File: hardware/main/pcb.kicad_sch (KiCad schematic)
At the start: 22 parts, among them J1 Conn_01x02_Socket, J2 Conn_01x02_Socket

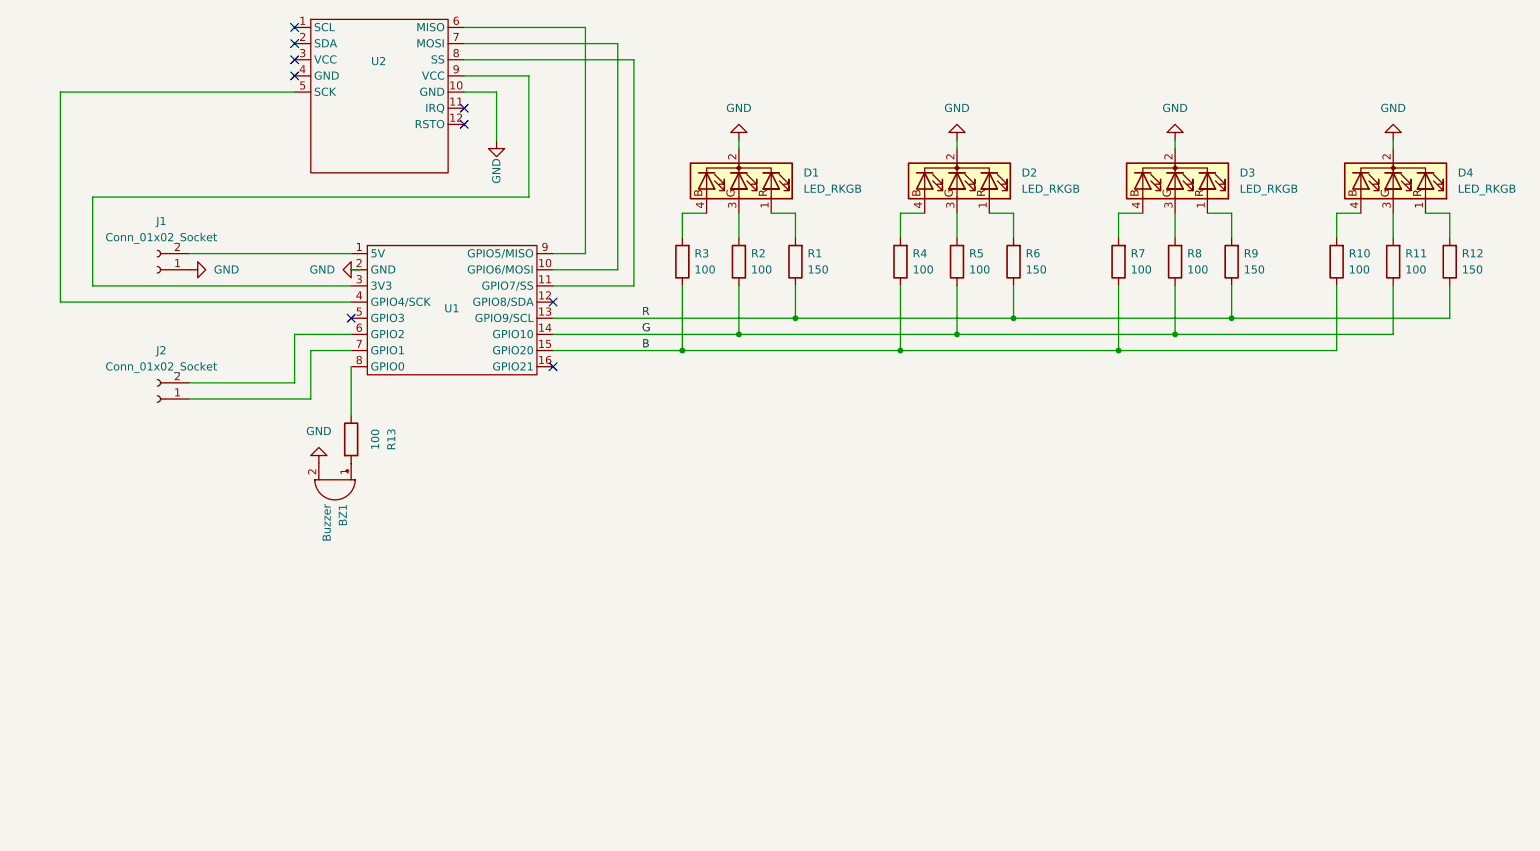
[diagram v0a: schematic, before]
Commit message: add trasistors to for led diode board
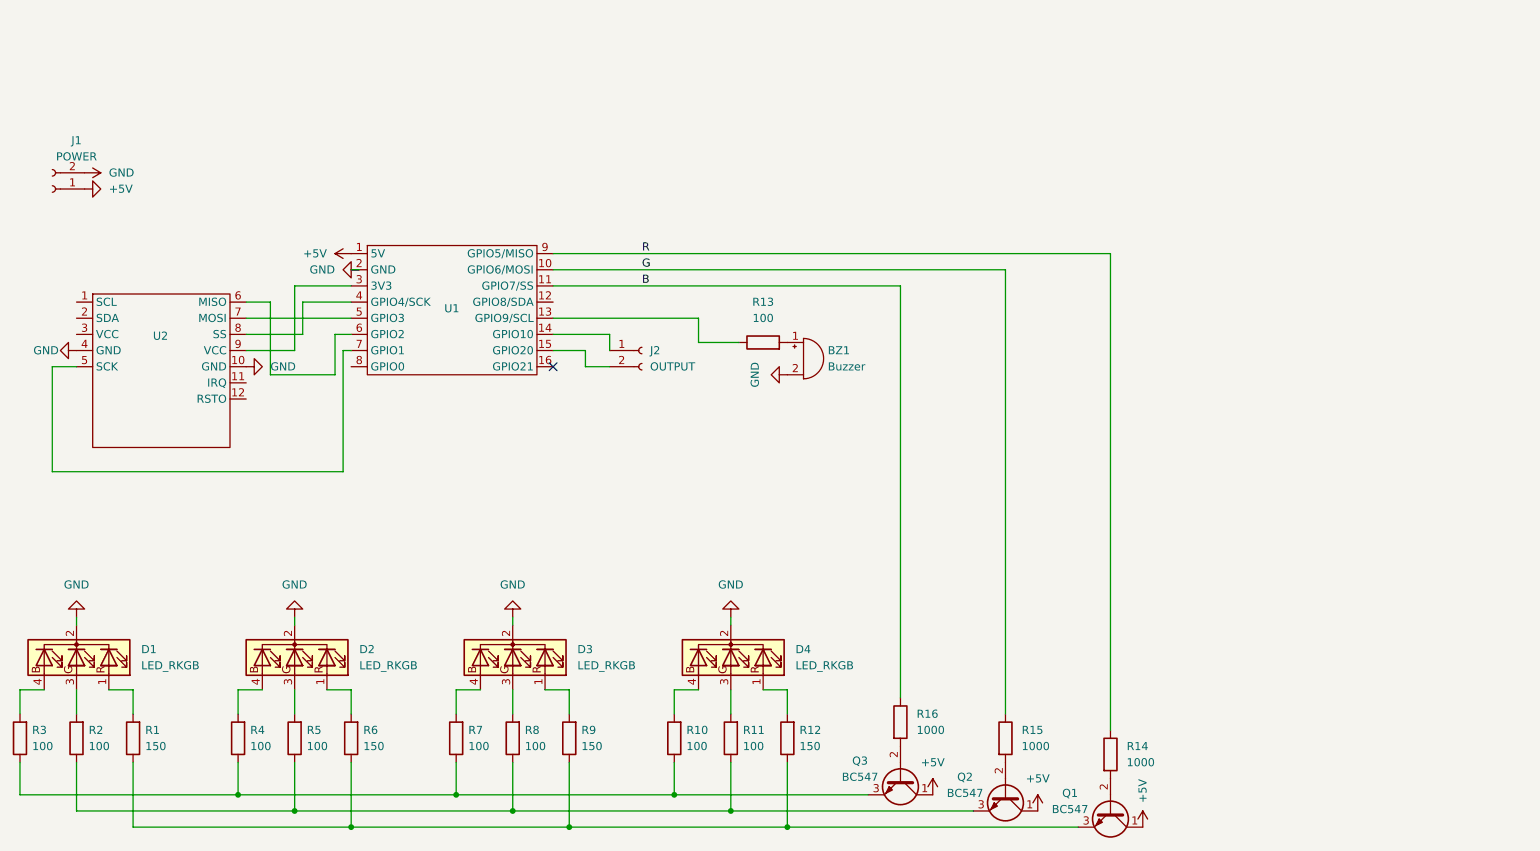
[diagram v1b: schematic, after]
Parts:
- added Q1, Q2, Q3: BC547, Package_TO_SOT_THT:TO-92_Inline, symbol Transistor_BJT:BC547
- added R14, R15, R16: 1000, Resistor_THT:CNC_Ready_R_Axial_DIN0204_L3.6mm_D1.6mm_P7.62mm_Horizontal, symbol Device:R
- J1: value Conn_01x02_Socket -> POWER; footprint TerminalBlock_Phoenix:TerminalBlock_Phoenix_MKDS-1,5-2-5.08_1x02_P5.08mm_Horizontal -> Connector_Molex:Molex_Nano-Fit_105313-xx02_1x02_P2.50mm_Horizontal
- J2: value Conn_01x02_Socket -> OUTPUT; footprint TerminalBlock_Phoenix:TerminalBlock_Phoenix_MKDS-1,5-2-5.08_1x02_P5.08mm_Horizontal -> Connector_Molex:Molex_Nano-Fit_105313-xx02_1x02_P2.50mm_Horizontal
- U1: footprint esp_32_c3_supper_mini:esp_32_c3_supper_mini_tht_smd -> esp_32_c3_supper_mini:esp_32_c3_supper_mini
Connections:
- net B: now also U1.11 (GPIO7/SS), R16.1; no longer R10.1, R3.1, R4.1, R7.1, U1.15 (GPIO20)
- net G: now also U1.10 (GPIO6/MOSI), R15.1; no longer R11.1, R2.1, R5.1, R8.1, U1.14 (GPIO10)
- net GND: now also J1.2 (Pin_2), U2.4 (GND); no longer J1.1 (Pin_1)
- net R: now also U1.9 (GPIO5/MISO), R14.1; no longer R1.1, R12.1, R6.1, R9.1, U1.13 (GPIO9/SCL)
- net at U2.5 (SCK): now also U1.7 (GPIO1); no longer U1.4 (GPIO4/SCK)
- net at U2.6 (MISO): now also U1.6 (GPIO2); no longer U1.9 (GPIO5/MISO)
- net at U2.7 (MOSI): now also U1.5 (GPIO3); no longer U1.10 (GPIO6/MOSI)
- net at U2.8 (SS): now also U1.4 (GPIO4/SCK); no longer U1.11 (GPIO7/SS)
- net at R13.1: now also U1.13 (GPIO9/SCL); no longer U1.8 (GPIO0)
- net +5V: now reaches U1.1 (5V)
- net +5V: now also J1.1 (Pin_1), Q1.1 (C), Q2.1 (C), Q3.1 (C); no longer J1.2 (Pin_2)
- net at J2.2 (Pin_2): now also U1.15 (GPIO20); no longer U1.6 (GPIO2)
- net at J2.1 (Pin_1): now also U1.14 (GPIO10); no longer U1.7 (GPIO1)
- new net: Q3.3 (E), R10.1, R3.1, R4.1, R7.1
- new net: Q1.3 (E), R1.1, R12.1, R6.1, R9.1
- new net: Q2.3 (E), R11.1, R2.1, R5.1, R8.1
- new net: Q3.2 (B), R16.2
- new net: Q2.2 (B), R15.2
- new net: Q1.2 (B), R14.2
- no-connect marks 9 -> 1
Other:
- moved on the sheet: BZ1, D1, D2, D3, D4, J1, J2, R1, R10, R11, R12, R13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

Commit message: update the pcb design
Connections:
- net B: now also U1.15 (GPIO20); no longer U1.11 (GPIO7/SS)
- net G: now also U1.14 (GPIO10); no longer U1.10 (GPIO6/MOSI)
- net R: now also U1.13 (GPIO9/SCL); no longer U1.9 (GPIO5/MISO)
- net at R13.1: no longer U1.13 (GPIO9/SCL)
- net at J2.1 (Pin_1): now also U1.10 (GPIO6/MOSI); no longer U1.14 (GPIO10)
- net at J2.2 (Pin_2): now also U1.9 (GPIO5/MISO); no longer U1.15 (GPIO20)
- no-connect marks 1 -> 2
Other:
- moved on the sheet: BZ1, J2, R13
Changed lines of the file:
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@@
 		(at 105.41 87.63)
 	)
+	(no_connect
+		(at 73.66 87.63)
+	)
 	(wire
 		(pts
@@
 	(wire
 		(pts
+			(xy 114.3 60.96) (xy 119.38 60.96)
+		)
+		(stroke
+			(width 0)
+			(type default)
+		)
+	)
+	(wire
+		(pts
 			(xy 55.88 149.86) (xy 55.88 154.94)
 		)
@@
 	(wire
 		(pts
-			(xy 105.41 74.93) (xy 160.02 74.93)
+			(xy 123.19 74.93) (xy 123.19 69.85)
 		)
 		(stroke
@@
 	(wire
 		(pts
-			(xy 64.77 85.09) (xy 57.15 85.09)
+			(xy 105.41 85.09) (xy 160.02 85.09)
 		)
 		(stroke
@@
 	(wire
 		(pts
-			(xy 128.27 138.43) (xy 124.46 138.43)
+			(xy 64.77 85.09) (xy 57.15 85.09)
 		)
 		(stroke
@@
 	(wire
 		(pts
-			(xy 133.35 157.48) (xy 171.45 157.48)
+			(xy 128.27 138.43) (xy 124.46 138.43)
 		)
 		(stroke
@@
 	(wire
 		(pts
-			(xy 73.66 85.09) (xy 72.39 85.09)
+			(xy 133.35 157.48) (xy 171.45 157.48)
 		)
 		(stroke
@@
 	(wire
 		(pts
-			(xy 105.41 85.09) (xy 110.49 85.09)
+			(xy 73.66 85.09) (xy 72.39 85.09)
 		)
 		(stroke
@@
 	(wire
 		(pts
-			(xy 105.41 69.85) (xy 193.04 69.85)
+			(xy 105.41 80.01) (xy 193.04 80.01)
 		)
 		(stroke
@@
 	(wire
 		(pts
-			(xy 69.85 138.43) (xy 73.66 138.43)
+			(xy 111.76 60.96) (xy 107.95 60.96)
 		)
 		(stroke
@@
 	(wire
 		(pts
-			(xy 128.27 80.01) (xy 128.27 83.82)
+			(xy 69.85 138.43) (xy 73.66 138.43)
 		)
 		(stroke
@@
 	(wire
 		(pts
-			(xy 105.41 80.01) (xy 128.27 80.01)
+			(xy 105.41 69.85) (xy 107.95 69.85)
 		)
 		(stroke
@@
 	(wire
 		(pts
-			(xy 64.77 127) (xy 64.77 128.27)
+			(xy 105.41 74.93) (xy 115.57 74.93)
 		)
 		(stroke
@@
 	(wire
 		(pts
-			(xy 105.41 82.55) (xy 114.3 82.55)
+			(xy 64.77 127) (xy 64.77 128.27)
 		)
 		(stroke
@@
 	(wire
 		(pts
-			(xy 110.49 85.09) (xy 110.49 87.63)
+			(xy 107.95 60.96) (xy 107.95 69.85)
 		)
 		(stroke
@@
 	(wire
 		(pts
-			(xy 128.27 83.82) (xy 134.62 83.82)
+			(xy 105.41 72.39) (xy 119.38 72.39)
 		)
 		(stroke
@@
 	(wire
 		(pts
-			(xy 105.41 72.39) (xy 176.53 72.39)
+			(xy 105.41 82.55) (xy 176.53 82.55)
 		)
 		(stroke
@@
 	(wire
 		(pts
+			(xy 123.19 69.85) (xy 127 69.85)
+		)
+		(stroke
+			(width 0)
+			(type default)
+		)
+	)
+	(wire
+		(pts
 			(xy 104.14 138.43) (xy 107.95 138.43)
 		)
@@
 	(wire
 		(pts
-			(xy 107.95 138.43) (xy 107.95 142.24)
+			(xy 119.38 60.96) (xy 119.38 72.39)
 		)
 		(stroke
@@
 	(wire
 		(pts
-			(xy 133.35 127) (xy 133.35 128.27)
+			(xy 107.95 138.43) (xy 107.95 142.24)
 		)
 		(stroke
@@
 	(wire
 		(pts
-			(xy 30.48 157.48) (xy 64.77 157.48)
+			(xy 133.35 127) (xy 133.35 128.27)
 		)
 		(stroke
@@
 	(wire
 		(pts
-			(xy 99.06 138.43) (xy 99.06 142.24)
+			(xy 30.48 157.48) (xy 64.77 157.48)
 		)
 		(stroke
@@
 	(wire
 		(pts
-			(xy 114.3 82.55) (xy 114.3 85.09)
+			(xy 99.06 138.43) (xy 99.06 142.24)
 		)
 		(stroke
@@
 	(wire
 		(pts
-			(xy 160.02 74.93) (xy 160.02 139.7)
+			(xy 39.37 160.02) (xy 73.66 160.02)
 		)
 		(stroke
@@
 	(wire
 		(pts
-			(xy 39.37 160.02) (xy 73.66 160.02)
+			(xy 118.11 74.93) (xy 123.19 74.93)
 		)
 		(stroke
@@
 	(wire
 		(pts
-			(xy 124.46 149.86) (xy 124.46 154.94)
+			(xy 160.02 85.09) (xy 160.02 139.7)
 		)
 		(stroke
@@
 	(wire
 		(pts
-			(xy 26.67 104.14) (xy 26.67 87.63)
+			(xy 124.46 149.86) (xy 124.46 154.94)
 		)
 		(stroke
@@
 	(wire
 		(pts
-			(xy 71.12 88.9) (xy 60.96 88.9)
+			(xy 26.67 104.14) (xy 26.67 87.63)
 		)
 		(stroke
@@
 	(wire
 		(pts
-			(xy 193.04 69.85) (xy 193.04 144.78)
+			(xy 193.04 80.01) (xy 193.04 144.78)
 		)
 		(stroke
@@
 	(wire
 		(pts
-			(xy 60.96 88.9) (xy 60.96 77.47)
+			(xy 176.53 82.55) (xy 176.53 142.24)
 		)
 		(stroke
@@
 	(wire
 		(pts
-			(xy 64.77 149.86) (xy 64.77 157.48)
+			(xy 71.12 88.9) (xy 60.96 88.9)
 		)
 		(stroke
@@
 	(wire
 		(pts
-			(xy 133.35 157.48) (xy 99.06 157.48)
+			(xy 60.96 88.9) (xy 60.96 77.47)
 		)
 		(stroke
@@
 	(wire
 		(pts
-			(xy 30.48 138.43) (xy 30.48 142.24)
+			(xy 64.77 149.86) (xy 64.77 157.48)
 		)
 		(stroke
@@
 	(wire
 		(pts
-			(xy 133.35 149.86) (xy 133.35 157.48)
+			(xy 133.35 157.48) (xy 99.06 157.48)
 		)
 		(stroke
@@
 	(wire
 		(pts
-			(xy 176.53 72.39) (xy 176.53 142.24)
+			(xy 30.48 138.43) (xy 30.48 142.24)
 		)
 		(stroke
@@
 	(wire
 		(pts
-			(xy 110.49 87.63) (xy 114.3 87.63)
+			(xy 133.35 149.86) (xy 133.35 157.48)
 		)
 		(stroke
@@
 	)
 	(label "G"
-		(at 119.38 72.39 0)
+		(at 120.65 82.55 0)
 		(effects
 			(font
@@
 	)
 	(label "R"
-		(at 119.38 69.85 0)
+		(at 120.65 80.01 0)
 		(effects
 			(font
@@
 	)
 	(label "B"
-		(at 119.38 74.93 0)
+		(at 120.65 85.09 0)
 		(effects
 			(font
@@
 	(symbol
 		(lib_id "Device:R")
-		(at 138.43 83.82 90)
+		(at 130.81 69.85 90)
 		(unit 1)
 		(exclude_from_sim no)
@@
 		(fields_autoplaced yes)
 		(property "Reference" "R13"
-			(at 138.43 77.47 90)
+			(at 130.81 63.5 90)
 			(effects
 				(font
@@
 		)
 		(property "Value" "100"
-			(at 138.43 80.01 90)
+			(at 130.81 66.04 90)
 			(effects
 				(font
@@
 		)
 		(property "Footprint" "Resistor_THT:CNC_Ready_R_Axial_DIN0204_L3.6mm_D1.6mm_P7.62mm_Horizontal"
-			(at 138.43 85.598 90)
+			(at 130.81 71.628 90)
 			(effects
 				(font
@@
 		)
 		(property "Datasheet" "~"
-			(at 138.43 83.82 0)
+			(at 130.81 69.85 0)
 			(effects
 				(font
@@
 		)
 		(property "Description" "Resistor"
-			(at 138.43 83.82 0)
+			(at 130.81 69.85 0)
 			(effects
 				(font
@@
 	(symbol
 		(lib_id "power:GND")
-		(at 142.24 88.9 270)
+		(at 134.62 74.93 270)
 		(unit 1)
 		(exclude_from_sim no)
@@
 		(dnp no)
 		(property "Reference" "#PWR08"
-			(at 135.89 88.9 0)
+			(at 128.27 74.93 0)
 			(effects
 				(font
@@
 		)
 		(property "Value" "GND"
-			(at 137.16 88.9 0)
+			(at 129.54 74.93 0)
 			(effects
 				(font
@@
 		)
 		(property "Footprint" ""
-			(at 142.24 88.9 0)
+			(at 134.62 74.93 0)
 			(effects
 				(font
@@
 		)
 		(property "Datasheet" ""
-			(at 142.24 88.9 0)
+			(at 134.62 74.93 0)
 			(effects
 				(font
@@
 		)
 		(property "Description" "Power symbol creates a global label with name \"GND\" , ground"
-			(at 142.24 88.9 0)
+			(at 134.62 74.93 0)
 			(effects
 				(font
@@
 	(symbol
 		(lib_id "Connector:Conn_01x02_Socket")
-		(at 119.38 85.09 0)
+		(at 114.3 66.04 270)
 		(unit 1)
 		(exclude_from_sim no)
@@
 		(fields_autoplaced yes)
 		(property "Reference" "J2"
-			(at 120.65 85.0899 0)
+			(at 115.57 64.1349 90)
 			(effects
 				(font
@@
 		)
 		(property "Value" "OUTPUT"
-			(at 120.65 87.6299 0)
+			(at 115.57 66.6749 90)
 			(effects
 				(font
@@
 		)
 		(property "Footprint" "Connector_Molex:Molex_Nano-Fit_105313-xx02_1x02_P2.50mm_Horizontal"
-			(at 119.38 85.09 0)
+			(at 114.3 66.04 0)
 			(effects
 				(font
@@
 		)
 		(property "Datasheet" "~"
-			(at 119.38 85.09 0)
+			(at 114.3 66.04 0)
 			(effects
 				(font
@@
 		)
 		(property "Description" "Generic connector, single row, 01x02, script generated"
-			(at 119.38 85.09 0)
+			(at 114.3 66.04 0)
 			(effects
 				(font
@@
 	(symbol
 		(lib_id "Device:Buzzer")
-		(at 144.78 86.36 0)
+		(at 137.16 72.39 0)
 		(unit 1)
 		(exclude_from_sim no)
@@
 		(fields_autoplaced yes)
 		(property "Reference" "BZ1"
-			(at 148.59 85.0899 0)
+			(at 140.97 71.1199 0)
 			(effects
 				(font
@@
 		)
 		(property "Value" "Buzzer"
-			(at 148.59 87.6299 0)
+			(at 140.97 73.6599 0)
 			(effects
 				(font
@@
 		)
 		(property "Footprint" "Buzzer_Beeper:MagneticBuzzer_ProSignal_ABI-010-RC"
-			(at 144.145 83.82 90)
+			(at 136.525 69.85 90)
 			(effects
 				(font
@@
 		)
 		(property "Datasheet" "~"
-			(at 144.145 83.82 90)
+			(at 136.525 69.85 90)
 			(effects
 				(font
@@
 		)
 		(property "Description" "Buzzer, polarized"
-			(at 144.78 86.36 0)
+			(at 137.16 72.39 0)
 			(effects
 				(font

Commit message: update the board
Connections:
- net at R13.1: now also U1.11 (GPIO7/SS)
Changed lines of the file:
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@@
 	(wire
 		(pts
-			(xy 105.41 74.93) (xy 115.57 74.93)
+			(xy 105.41 74.93) (xy 123.19 74.93)
 		)
 		(stroke
@@
 		)
 		(stroke
-			(width 0)
-			(type default)
-		)
-	)
-	(wire
-		(pts
-			(xy 118.11 74.93) (xy 123.19 74.93)
-		)
-		(stroke

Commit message: Update the pcb (#45)
* add tag emular tool

* fix the buzzer

* update pcb

* update the pcb
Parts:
- removed J2: OUTPUT, Connector_Molex:Molex_Nano-Fit_105313-xx02_1x02_P2.50mm_Horizontal, symbol Connector:Conn_01x02_Socket
- added J3: Conn_01x03_Socket, Connector_PinSocket_2.54mm:PinSocket_1x03_P2.54mm_Vertical_with_holes, symbol Connector:Conn_01x03_Socket
- J1: value POWER -> Conn_01x02_Socket; footprint Connector_Molex:Molex_Nano-Fit_105313-xx02_1x02_P2.50mm_Horizontal -> Connector_PinSocket_2.54mm:PinSocket_2x01_P2.54mm_Vertical
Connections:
- net +5V: now also J3.1 (Pin_1)
- net GND: now also J3.2 (Pin_2); no longer U2.4 (GND)
- net at U1.9 (GPIO5/MISO): now also J3.3 (Pin_3)
- no-connect marks 2 -> 9
